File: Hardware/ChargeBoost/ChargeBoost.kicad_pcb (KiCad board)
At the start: 2 copper layers, 84.8 x 20.9 mm, 31 parts, among them J1 USB4125-GF-A_REVA2, J3 Conn_01x01_Male, J4 Conn_01x01_Male, J5 Conn_01x01_Male, SW1 SW_Push, SW2 PWR, U1 TPS61235PRWLT, U2 MCP73871-2AAI_ML

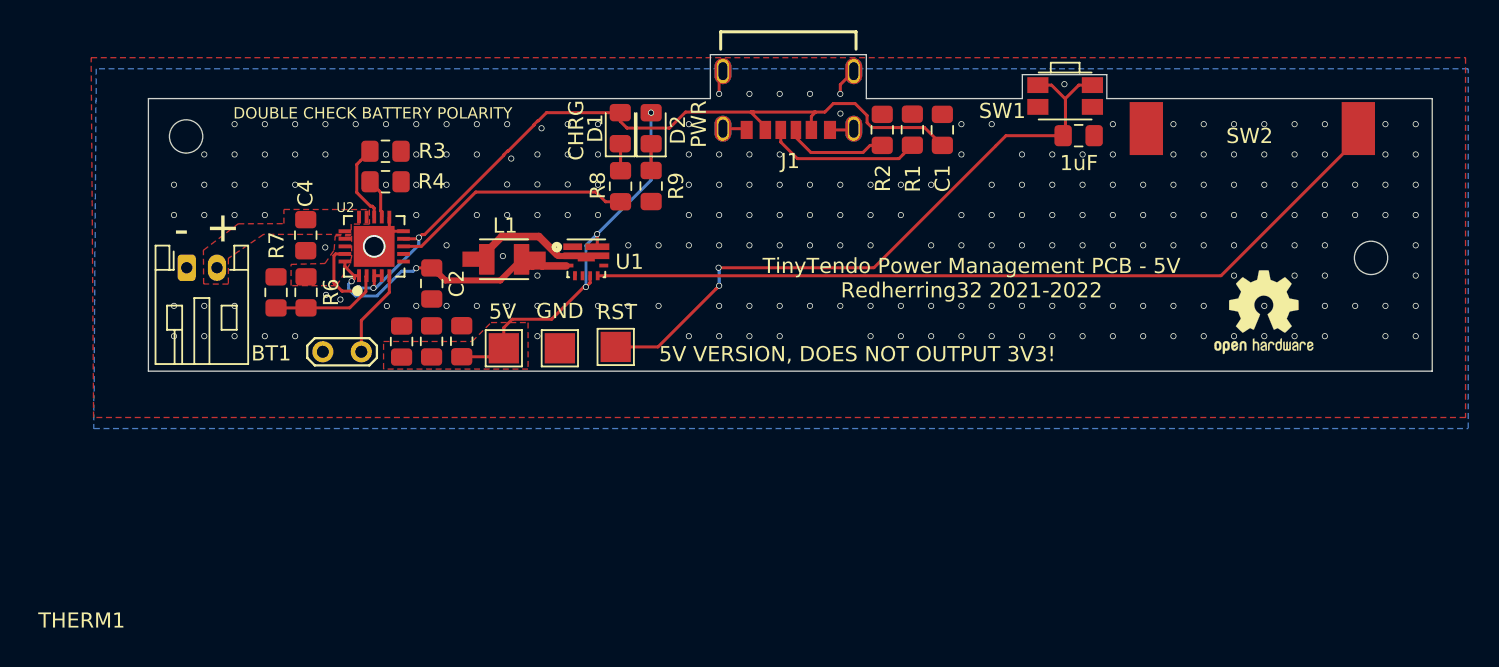
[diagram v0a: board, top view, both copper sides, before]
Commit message: Redid ChargeBoost layout, and added EN pull up, and RST capacitor
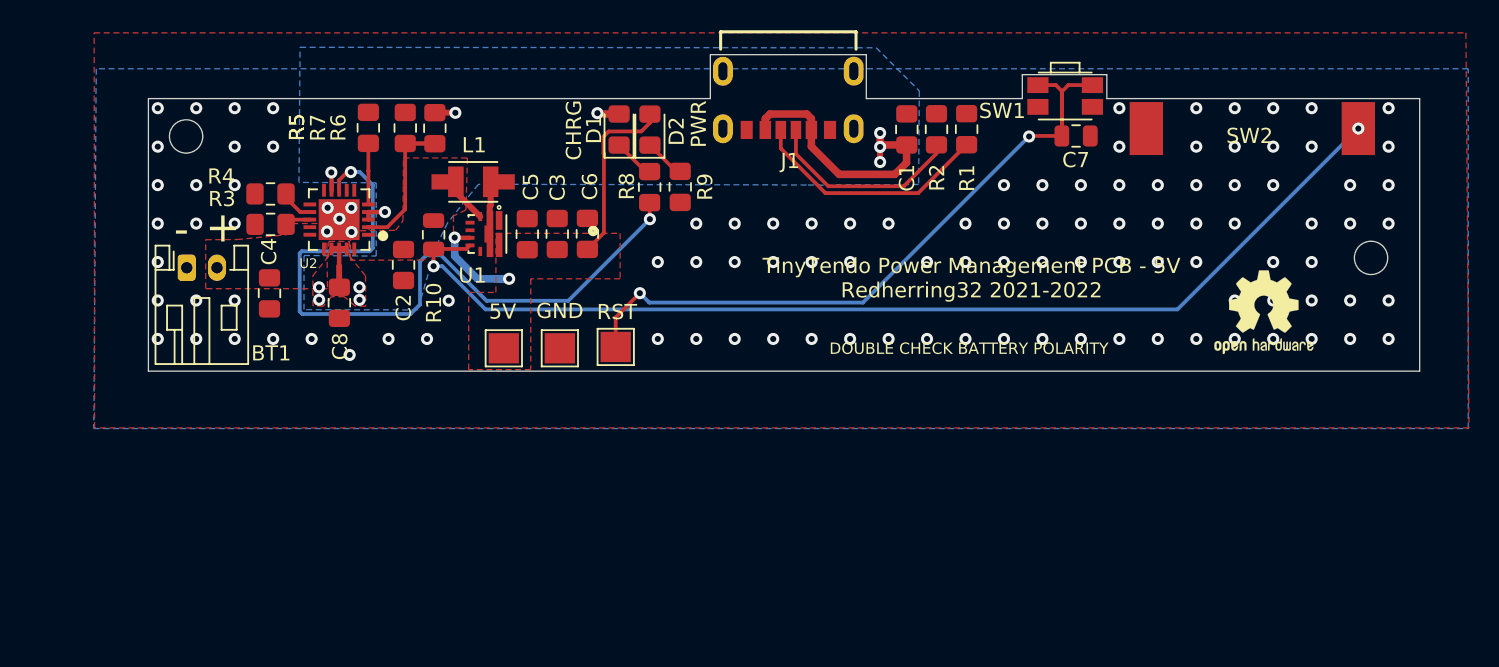
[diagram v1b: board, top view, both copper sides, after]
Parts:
- removed the   at (95.5, 24.8)
- added C7: 1uF, Capacitor_SMD:C_0805_2012Metric, F.Cu at (95.3, 24.8)
- added C8: 10uF, Capacitor_SMD:C_0805_2012Metric_Pad1.15x1.40mm_HandSolder, F.Cu at (46.7, 35.8)
- added R10: 200R, Resistor_SMD:R_0805_2012Metric, F.Cu at (52.9, 31.3)
- R5: renamed from THERM1; footprint TestPoint:TestPoint_2Pads_Pitch2.54mm_Drill0.8mm -> Resistor_SMD:R_0805_2012Metric_Pad1.15x1.40mm_HandSolder
- moved R5 14.8 mm to (48.6, 24.2), turned to 90 degrees
- moved R7 13.8 mm to (51.0, 24.2)
- moved R6 13.8 mm to (53.0, 24.3)
- moved C6 10.9 mm to (63.0, 31.2)
- moved C3 10.9 mm to (61.0, 31.2)
- moved C5 10.9 mm to (59.1, 31.3)
- moved R3 8.99 mm to (42.1, 30.6), turned to 180 degrees
- moved R4 7.64 mm to (42.1, 28.6), turned to 180 degrees
- moved U1 6.72 mm to (56.4, 31.2), turned to 270 degrees
- moved L1 5.50 mm to (55.5, 27.8), turned to 0 degrees
- moved C4 4.53 mm to (42.0, 35.2)
- moved R1 3.58 mm to (88.1, 24.3)
- moved R2 3.58 mm to (86.1, 24.3)
- moved U2 2.91 mm to (46.6, 30.3), turned to 180 degrees
- moved C1 2.35 mm to (84.1, 24.3)
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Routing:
- net Net-(R8-Pad2): track 16.1 -> 47.7 mm, vias 0 -> 2
- net /VBUS: track 57.0 -> 27.3 mm, vias 3 -> 11
- net Net-(R10-Pad2): track 54.6 -> 70.8 mm, vias 0 -> 2
- net /VBAT: track 19.0 -> 2.96 mm, vias 2 -> 0
- net /GND: track 10.9 -> 0.00 mm, vias 232 -> 111
- net /VOUT: track 25.9 -> 19.3 mm, vias 3 -> 2
- net Net-(J1-PadA5): track 6.80 -> 13.2 mm
- net Net-(J1-PadB5): track 10.3 -> 16.0 mm
- net Net-(L1-Pad2): track 8.03 -> 3.86 mm
- net Net-(R3-Pad1): track 5.25 -> 1.70 mm
- net /RST: track 43.4 -> 46.7 mm
- net Net-(R6-Pad2): track 6.78 -> 9.92 mm
- net Net-(R5-Pad1): track 5.79 -> 4.04 mm
- net Net-(D2-Pad1): track 1.77 -> 3.31 mm
- net Net-(D1-Pad1): track 1.79 -> 2.97 mm
- added copper zone on F.Cu, net /VBAT
- added copper zone on B.Cu, net /VBUS
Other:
- board size 84.8 x 20.9 mm -> 84 x 20.9 mm
- board text removed: "5V VERSION, DOES NOT OUTPUT 3V3!"
